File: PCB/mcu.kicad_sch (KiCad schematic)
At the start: 33 parts, among them J5 Conn_01x02, SW1 Boot, SW2 Reset, U4 ESP32-C3FH4X, Y1 40MHz

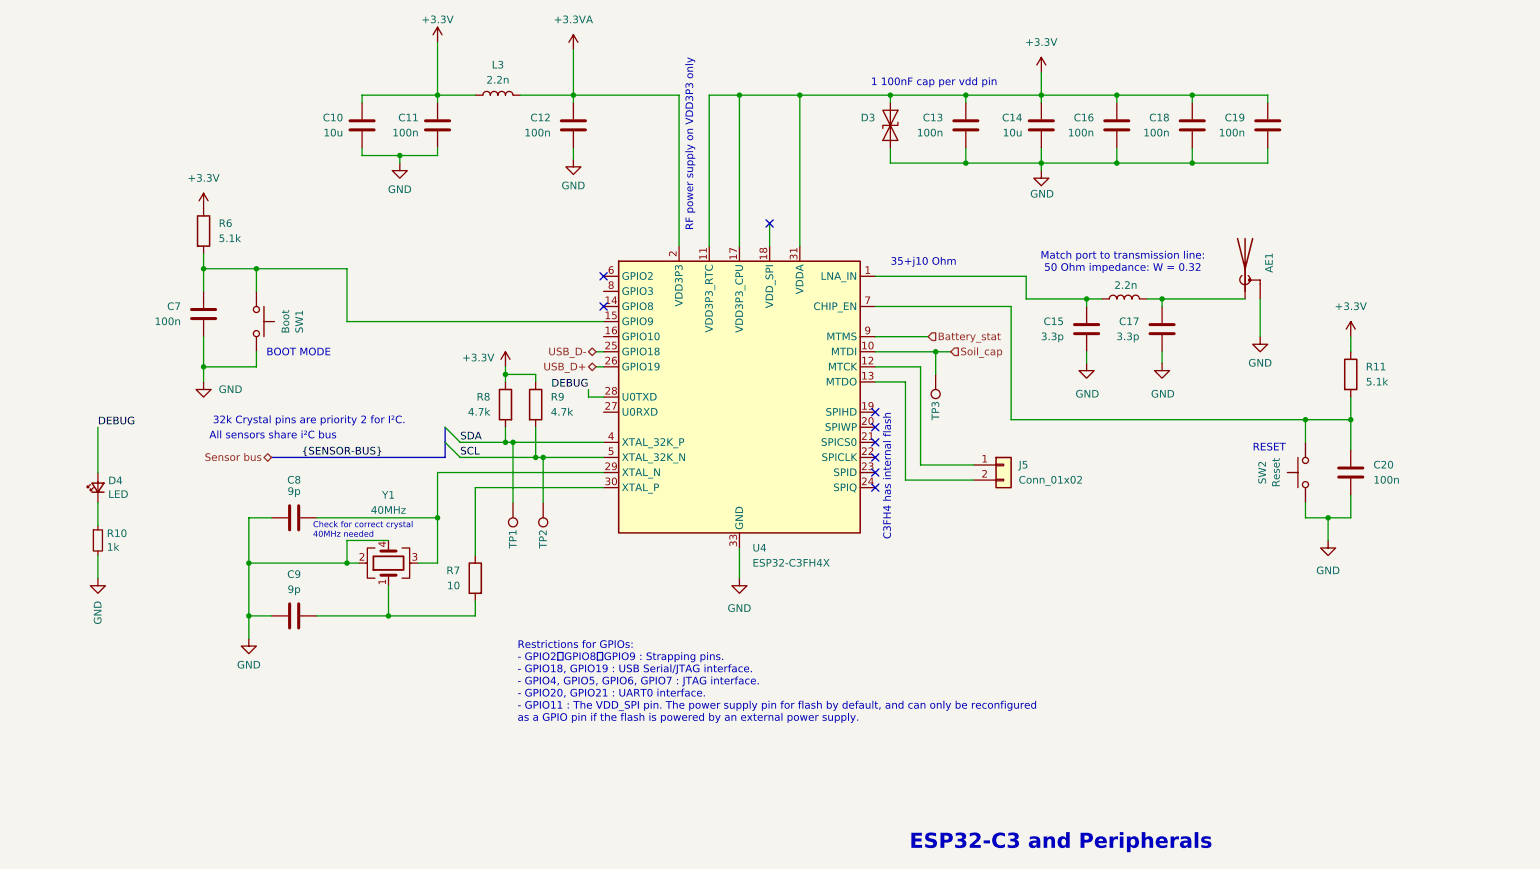
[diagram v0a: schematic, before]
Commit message: Added light sensor simulation and schematic
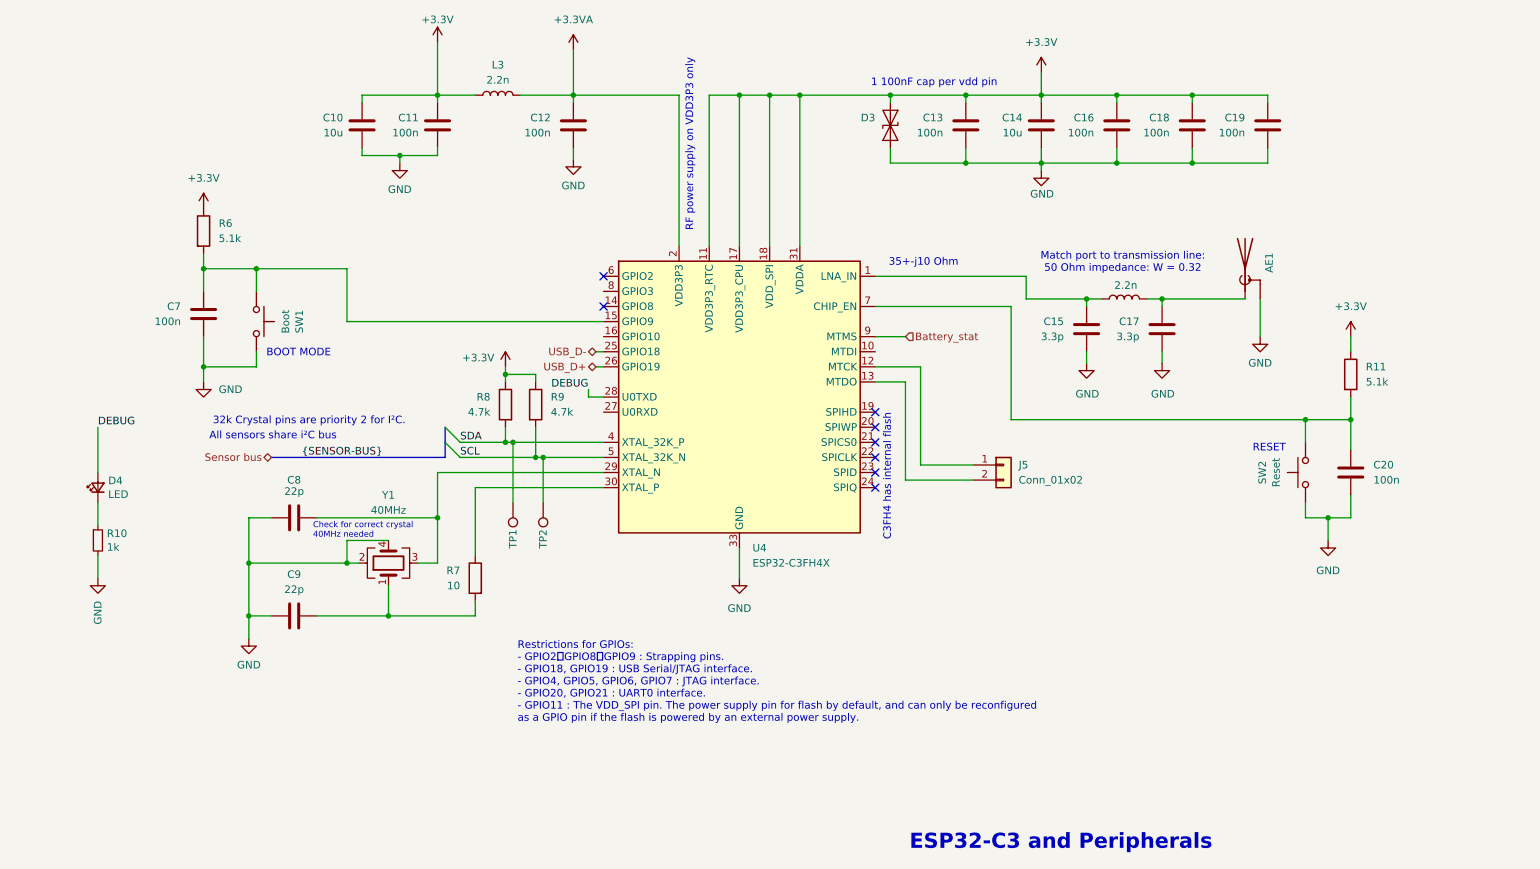
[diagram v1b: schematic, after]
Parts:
- removed TP3: TestPoint, TestPoint:TestPoint_Pad_D1.0mm, symbol Connector:TestPoint
- C8, C9: value 9p -> 22p
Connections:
- net +3.3V: now also U4.18 (VDD_SPI)
- net Soil_cap: no longer names the net of U4.10 (MTDI)
- no-connect marks 9 -> 8
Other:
- note added: "35+-j10 Ohm"
- note removed: "35+j10 Ohm"

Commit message: Light sensor
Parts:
- C15, C17: value 3.3p -> 2.2p
- L4: value 2.2n -> 2.6n
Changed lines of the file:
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@@
 	(text "Match port to transmission line:\n50 Ohm impedance: W = 0.32"
 		(exclude_from_sim no)
-		(at 215.646 76.454 0)
+		(at 210.312 75.692 0)
 		(effects
 			(font
@@
 			)
 		)
-		(property "Value" "3.3p"
+		(property "Value" "2.2p"
 			(at 205.74 88.9 0)
 			(effects
@@
 			)
 		)
-		(property "Value" "2.2n"
+		(property "Value" "2.6n"
 			(at 216.154 80.264 90)
 			(effects
@@
 			)
 		)
-		(property "Value" "3.3p"
+		(property "Value" "2.2p"
 			(at 218.44 88.9 0)
 			(effects

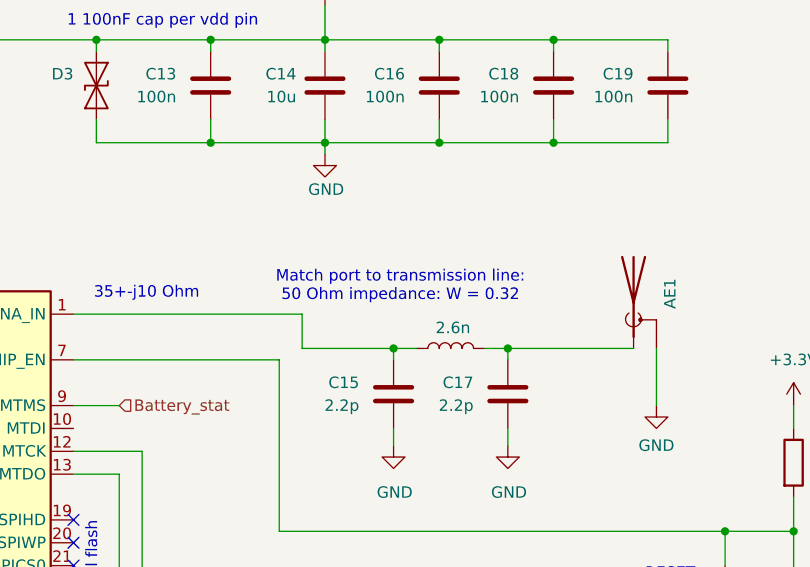
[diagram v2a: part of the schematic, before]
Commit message: removed usb port library
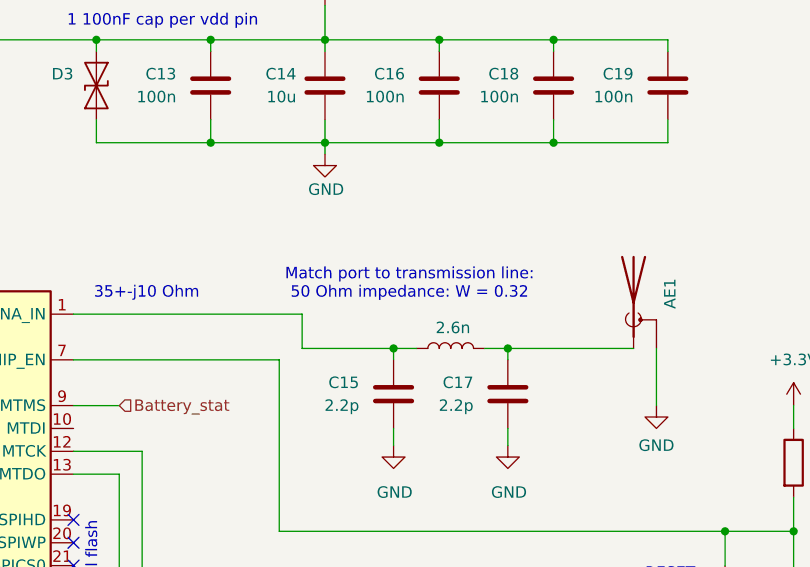
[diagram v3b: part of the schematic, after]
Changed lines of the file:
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@@
 	(text "Match port to transmission line:\n50 Ohm impedance: W = 0.32"
 		(exclude_from_sim no)
-		(at 210.312 75.692 0)
+		(at 211.328 75.438 0)
 		(effects
 			(font

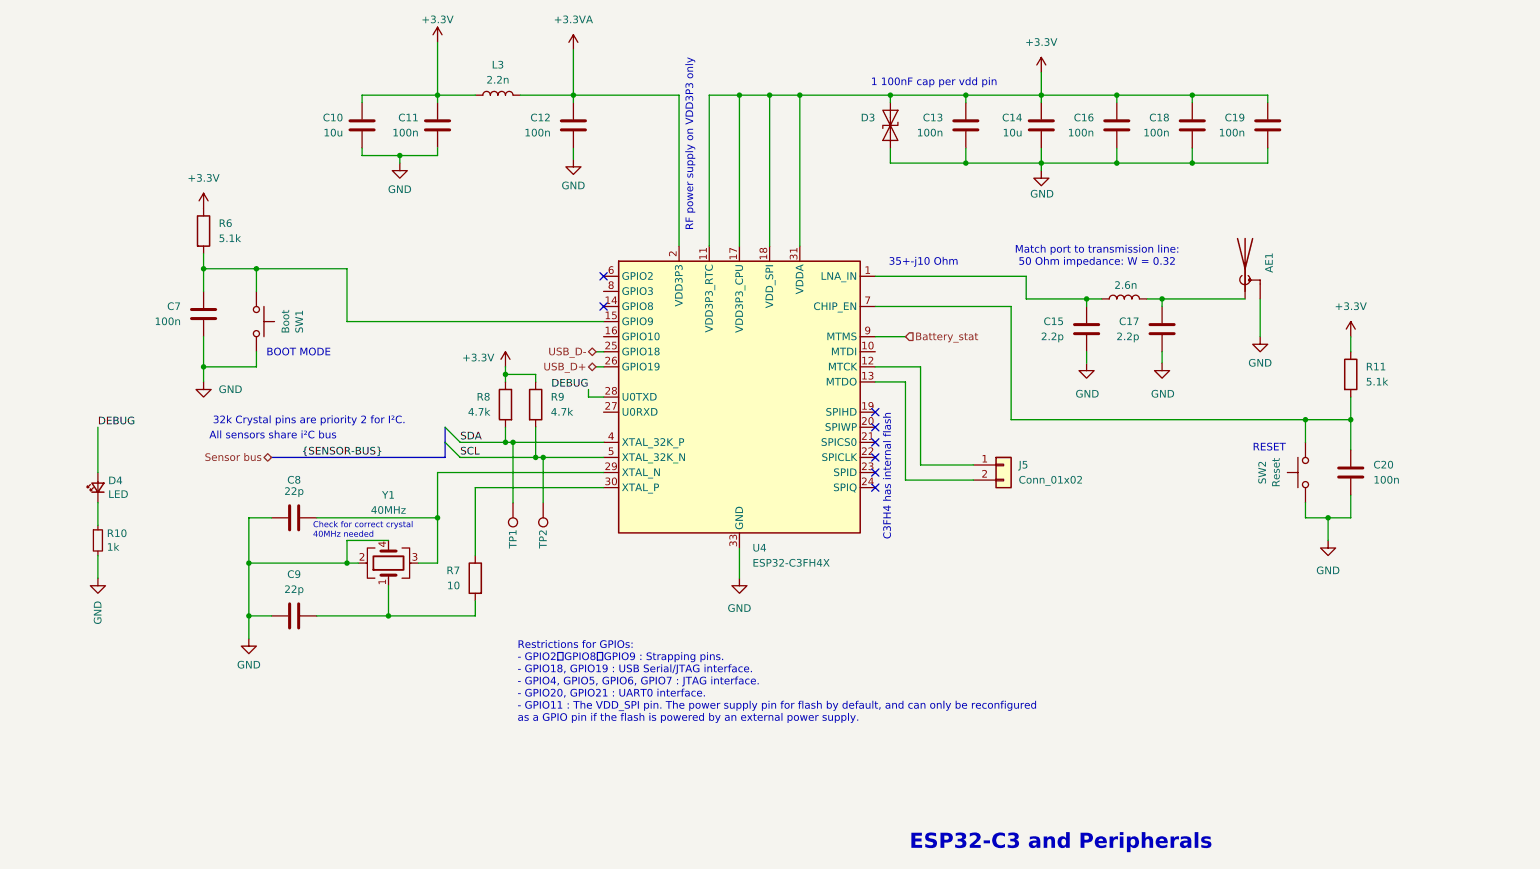
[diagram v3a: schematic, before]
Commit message: Optimized PCB lauout and added Header for LED indicator bar
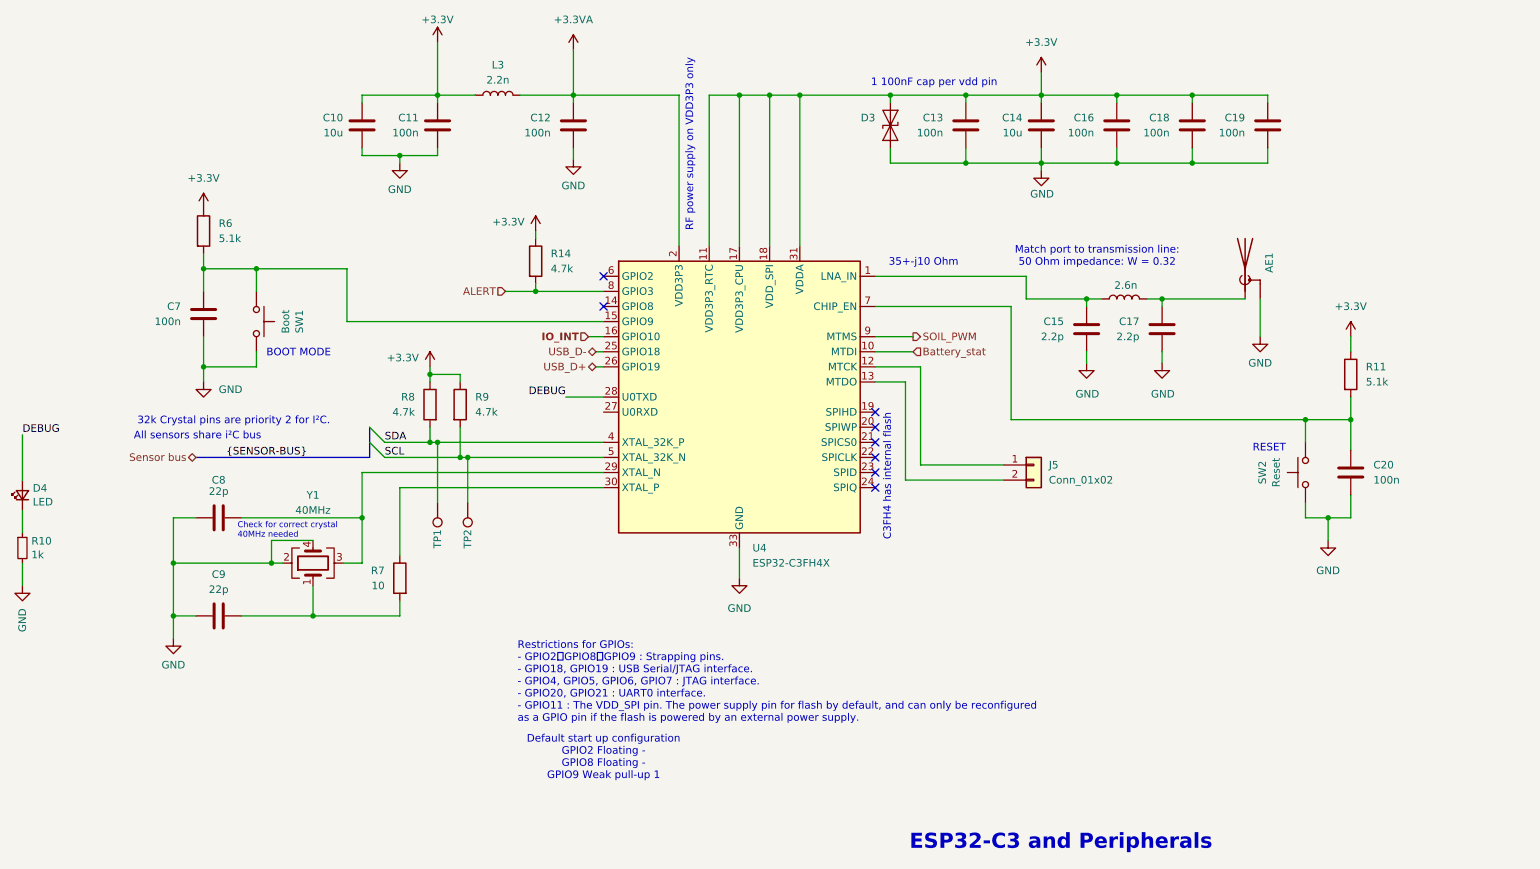
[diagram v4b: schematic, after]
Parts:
- added R14: 4.7k, Resistor_SMD:R_0402_1005Metric, symbol Device:R
- AE1: footprint RF_Antenna:Texas_SWRA117D_2.4GHz_Right -> RF_Antenna:Texas_SWRA117D_2.4GHz_Left
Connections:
- net +3.3V: now also R14.1
- net Battery_stat: now also U4.10 (MTDI); no longer U4.9 (MTMS)
- net IO_INT: now reaches U4.16 (GPIO10)
- net ALERT: now reaches U4.8 (GPIO3)
- net ALERT: now also R14.2
- new net SOIL_PWM: U4.9 (MTMS)
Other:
- note added: "Default start up configuration GPIO2 Floating - GPIO8 Floating - GPIO9 Weak pull-up 1"
- moved on the sheet: C8, C9, D4, J5, R10, R7, R8, R9, TP1, TP2, Y1

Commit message: Finished PCB routing and added reference designators
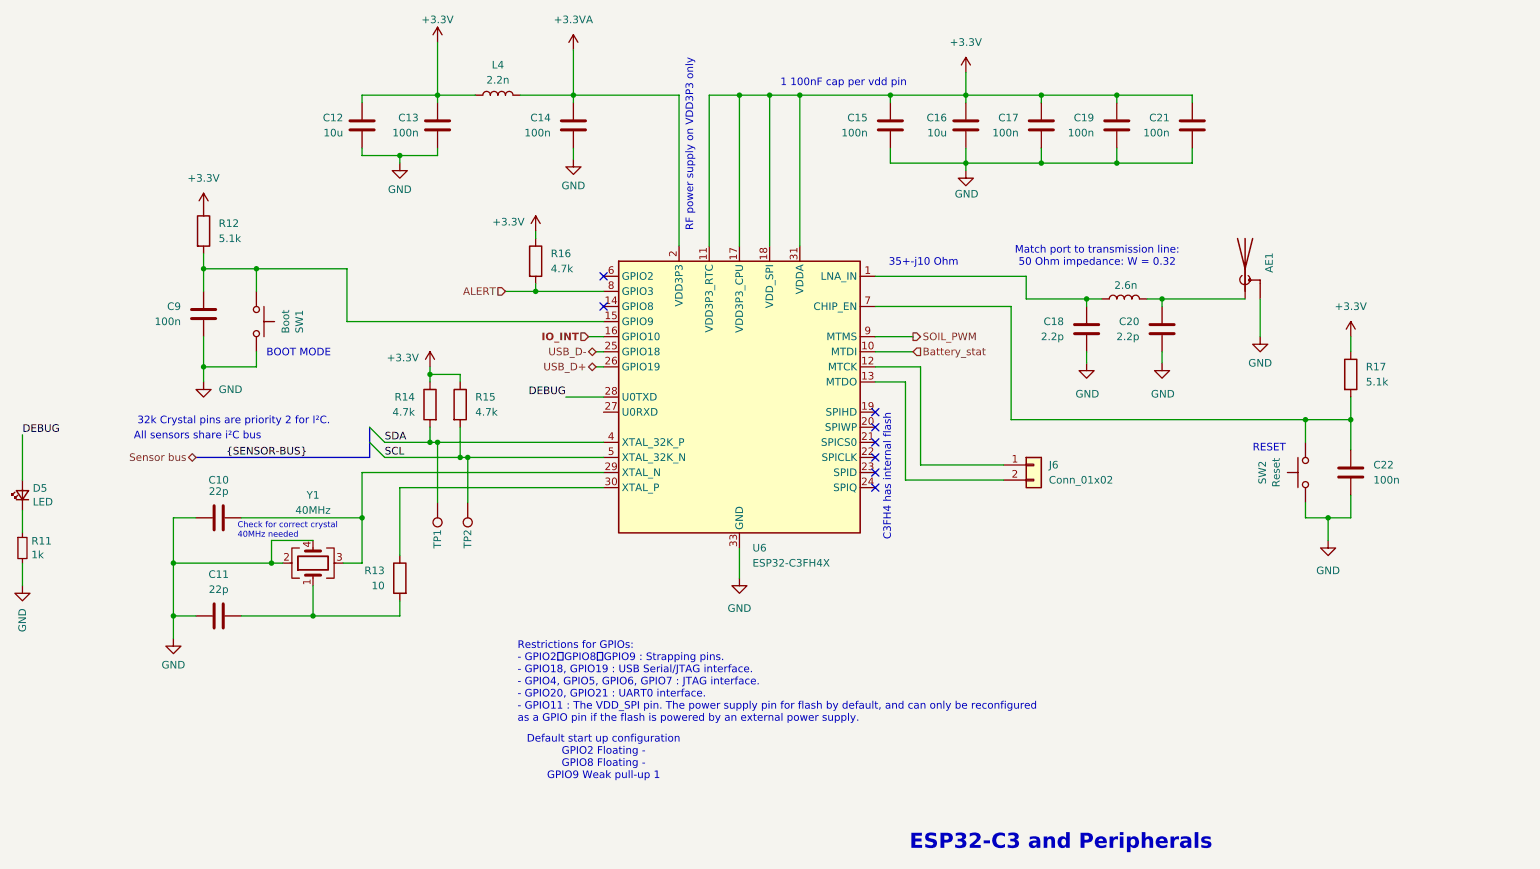
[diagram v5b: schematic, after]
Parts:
- removed D3: SZESD9B5.0ST5G, Diode_SMD:D_SOD-923, symbol Diode:SZESD9B5.0ST5G
- renumbered C8 to C10, C9 to C11, C10 to C12, C11 to C13, C12 to C14, C13 to C15, C14 to C16, C16 to C17, C15 to C18, C18 to C19, C17 to C20, C19 to C21, C20 to C22, C7 to C9, D4 to D5, J5 to J6, L3 to L4, L4 to L5, R10 to R11, R6 to R12, R7 to R13, R8 to R14, R9 to R15, R14 to R16, R11 to R17, U4 to U6
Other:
- moved on the sheet: C15, C16, C17, C19, C21

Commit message: Final touches to PCB
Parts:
- added J8: Conn_01x02, Connector_PinHeader_2.54mm:PinHeader_1x02_P2.54mm_Vertical, symbol Connector_Generic:Conn_01x02
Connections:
- no-connect marks 8 -> 9
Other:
- note added: "C3FH4 has internal flash DO NOT CONNECT!"
- note removed: "C3FH4 has internal flash"
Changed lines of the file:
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@@
 		)
 	)
-	(text "C3FH4 has internal flash"
+	(text "C3FH4 has internal flash\nDO NOT CONNECT!"
 		(exclude_from_sim no)
-		(at 176.022 112.522 90)
+		(at 177.546 109.474 90)
 		(effects
 			(font
@@
 	)
 	(no_connect
+		(at 128.27 101.6)
+	)
+	(no_connect
 		(at 173.99 106.68)
 	)
@@
 	(wire
 		(pts
-			(xy 125.73 88.9) (xy 128.27 88.9)
+			(xy 127 88.9) (xy 128.27 88.9)
 		)
 		(stroke
@@
 	(wire
 		(pts
-			(xy 181.61 110.49) (xy 195.58 110.49)
+			(xy 184.15 110.49) (xy 195.58 110.49)
 		)
 		(stroke
@@
 	(wire
 		(pts
-			(xy 179.07 96.52) (xy 179.07 113.03)
+			(xy 181.61 96.52) (xy 181.61 113.03)
 		)
 		(stroke
@@
 	(wire
 		(pts
-			(xy 173.99 96.52) (xy 179.07 96.52)
+			(xy 173.99 96.52) (xy 181.61 96.52)
 		)
 		(stroke
@@
 	(wire
 		(pts
-			(xy 179.07 113.03) (xy 195.58 113.03)
+			(xy 181.61 113.03) (xy 195.58 113.03)
 		)
 		(stroke
@@
 	(wire
 		(pts
-			(xy 173.99 93.98) (xy 181.61 93.98)
+			(xy 173.99 93.98) (xy 184.15 93.98)
 		)
 		(stroke
@@
 	(wire
 		(pts
-			(xy 181.61 93.98) (xy 181.61 110.49)
+			(xy 184.15 93.98) (xy 184.15 110.49)
 		)
 		(stroke
@@
 	(hierarchical_label "IO_INT"
 		(shape input)
-		(at 125.73 88.9 180)
+		(at 127 88.9 180)
 		(effects
 			(font
 				(size 1.27 1.27)
-				(thickness 0.254)
-				(bold yes)
+				(thickness 0.1588)
 			)
 			(justify right)
@@
 					(unit 1)
 				)
+			)
+		)
+	)
+	(symbol
+		(lib_id "Connector_Generic:Conn_01x02")
+		(at 116.84 130.81 180)
+		(unit 1)
+		(exclude_from_sim no)
+		(in_bom yes)
+		(on_board yes)
+		(dnp no)
+		(fields_autoplaced yes)
+		(property "Reference" "J8"
+			(at 116.84 121.92 0)
+			(effects
+				(font
+					(size 1.27 1.27)
+				)
+			)
+		)
+		(property "Value" "Conn_01x02"
+			(at 116.84 124.46 0)
+			(effects
+				(font
+					(size 1.27 1.27)
+				)
+			)
+		)
+		(property "Footprint" "Connector_PinHeader_2.54mm:PinHeader_1x02_P2.54mm_Vertical"
+			(at 116.84 130.81 0)
+			(effects
+				(font
+					(size 1.27 1.27)
+				)
+				(hide yes)
+			)
+		)
+		(property "Datasheet" "~"
+			(at 116.84 130.81 0)
+			(effects
+				(font
+					(size 1.27 1.27)
+				)
+				(hide yes)
+			)
+		)
+		(property "Description" "Generic connector, single row, 01x02, script generated (kicad-library-utils/schlib/autogen/connector/)"
+			(at 116.84 130.81 0)
+			(effects
+				(font
+					(size 1.27 1.27)
+				)
+				(hide yes)
+			)
+		)
+		(pin "1"
+		)
+		(pin "2"
+		)
+		(instances
+			(project "Plant-health-meter"
+				(path "/357055bf-c309-4d6b-a2fa-f5ee5ba59771/f878f43f-0ef0-4ca5-9286-ff16b4b716af"
+					(reference "J8")
+					(unit 1)
+				)
